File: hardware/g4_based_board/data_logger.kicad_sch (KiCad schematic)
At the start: 32 parts, among them J1 USB_C_Receptacle_USB2.0, SW1 SW_SPDT, SW2 RESET, U1 STM32G431CBTx, U2 AZ1117-3.3, Y1 12MHz, 20pF

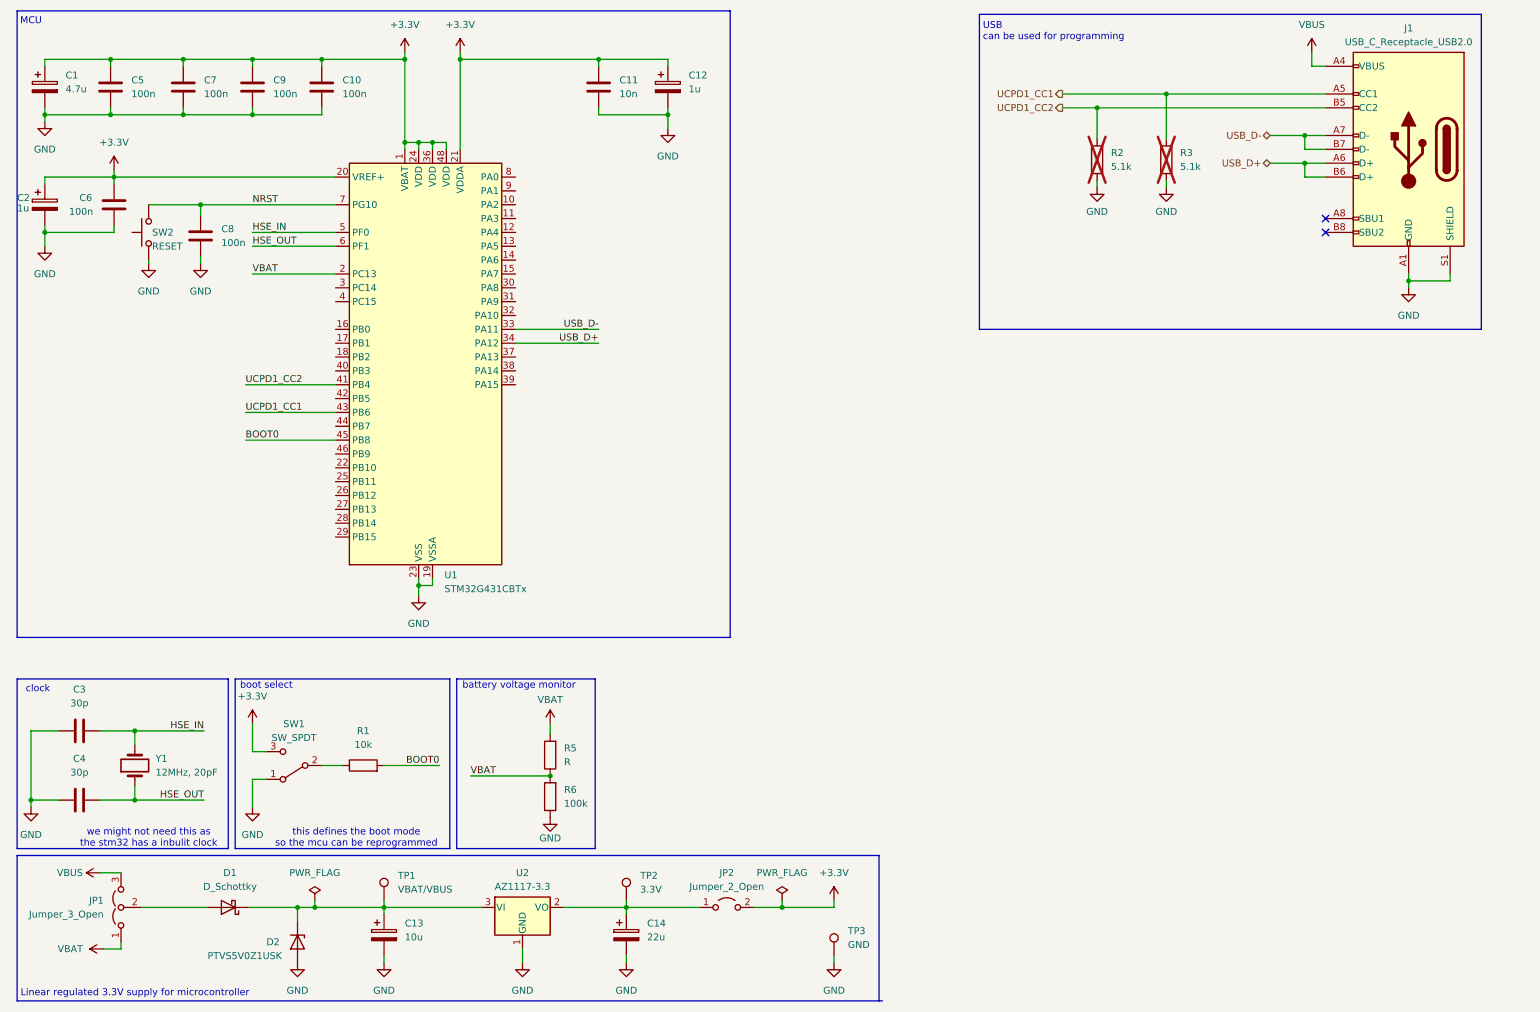
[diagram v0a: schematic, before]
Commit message: added auto updated files
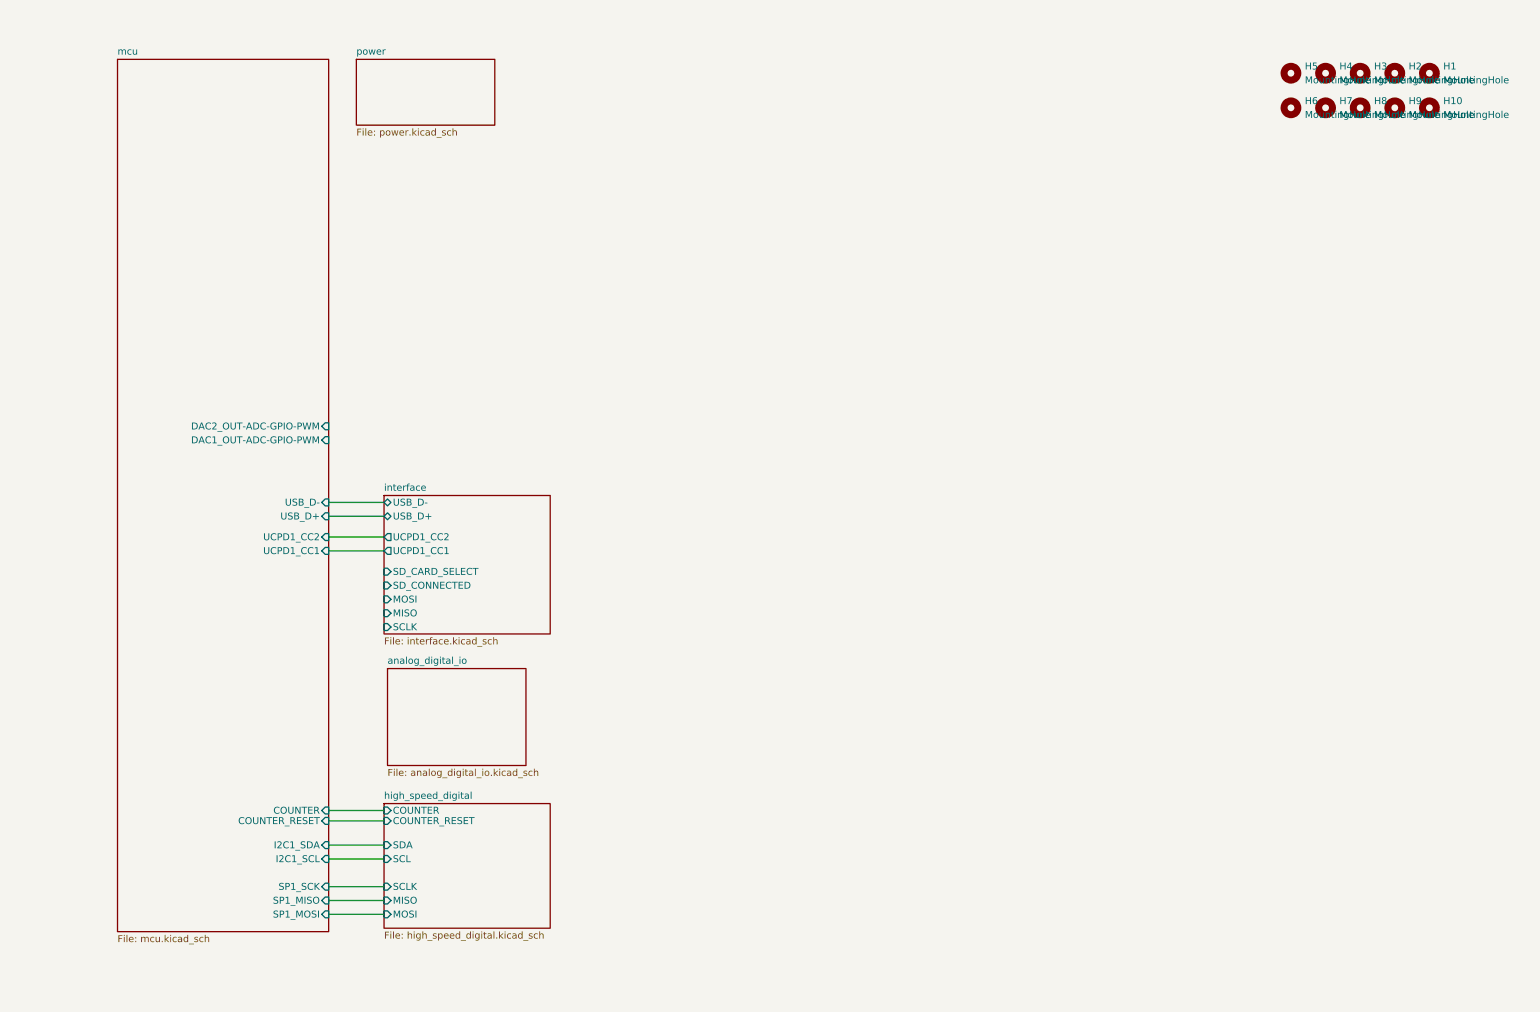
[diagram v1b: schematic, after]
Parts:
- removed C1: 4.7u, Capacitor_SMD:C_0805_2012Metric_Pad1.18x1.45mm_HandSolder, symbol Device:C_Polarized
- removed C10, C5, C6, C7, C8, C9: 100n, Capacitor_SMD:C_0805_2012Metric_Pad1.18x1.45mm_HandSolder, symbol Device:C
- removed C11: 10n, Capacitor_SMD:C_0805_2012Metric_Pad1.18x1.45mm_HandSolder, symbol Device:C
- removed C12, C2: 1u, Capacitor_SMD:C_0805_2012Metric_Pad1.18x1.45mm_HandSolder, symbol Device:C_Polarized
- removed C13: 10u, Capacitor_SMD:C_0805_2012Metric_Pad1.18x1.45mm_HandSolder, symbol Device:C_Polarized
- removed C14: 22u, Capacitor_SMD:C_0805_2012Metric_Pad1.18x1.45mm_HandSolder, symbol Device:C_Polarized
- removed C3, C4: 30p, Capacitor_SMD:C_0805_2012Metric_Pad1.18x1.45mm_HandSolder, symbol Device:C
- removed D1: D_Schottky, Diode_SMD:D_0805_2012Metric_Pad1.15x1.40mm_HandSolder, symbol Device:D_Schottky
- removed D2: PTVS5V0Z1USK, Diode_SMD:Nexperia_DSN1608-2_1.6x0.8mm, symbol Diode:PTVS5V0Z1USK
- removed J1: USB_C_Receptacle_USB2.0, Connector_USB:USB_C_Receptacle_HRO_TYPE-C-31-M-12, symbol Connector:USB_C_Receptacle_USB2.0
- removed JP1: Jumper_3_Open, Connector_PinHeader_2.54mm:PinHeader_1x03_P2.54mm_Vertical, symbol Jumper:Jumper_3_Open
- removed JP2: Jumper_2_Open, symbol Jumper:Jumper_2_Open
- removed R1: 10k, Resistor_SMD:R_0805_2012Metric_Pad1.20x1.40mm_HandSolder, symbol Device:R
- removed R2, R3: 5.1k, Resistor_SMD:R_0805_2012Metric_Pad1.20x1.40mm_HandSolder, symbol Device:R
- removed R5: R, Resistor_SMD:R_0805_2012Metric_Pad1.20x1.40mm_HandSolder, symbol Device:R
- removed R6: 100k, Resistor_SMD:R_0805_2012Metric_Pad1.20x1.40mm_HandSolder, symbol Device:R
- removed SW1: SW_SPDT, Button_Switch_THT:SW_Slide_SPDT_Angled_CK_OS102011MA1Q, symbol Switch:SW_SPDT
- removed SW2: RESET, Button_Switch_SMD:SW_Push_SPST_NO_Alps_SKRK, symbol Switch:SW_Push
- removed TP1: VBAT/VBUS, TestPoint:TestPoint_Pad_D1.5mm, symbol Connector:TestPoint
- removed TP2: 3.3V, TestPoint:TestPoint_Pad_D1.5mm, symbol Connector:TestPoint
- removed TP3: GND, TestPoint:TestPoint_Pad_D1.5mm, symbol Connector:TestPoint
- removed U1: STM32G431CBTx, Package_QFP:LQFP-48_7x7mm_P0.5mm, symbol MCU_ST_STM32G4:STM32G431CBTx
- removed U2: AZ1117-3.3, Package_TO_SOT_SMD:SOT-223, symbol Regulator_Linear:AZ1117-3.3
- removed Y1: 12MHz, 20pF, Crystal:Crystal_HC49-U_Vertical, symbol Device:Crystal
- added H1, H10, H2, H3, H4, H5, H6, H7, H8, H9: MountingHole, MountingHole:MountingHole_3.2mm_M3, symbol Mechanical:MountingHole
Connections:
- no-connect marks 2 -> 0
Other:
- added sheet analog_digital_io (analog_digital_io.kicad_sch)
- added sheet high_speed_digital (high_speed_digital.kicad_sch)
- added sheet interface (interface.kicad_sch)
- added sheet mcu (mcu.kicad_sch)
- added sheet power (power.kicad_sch)
- note removed: "Linear regulated 3.3V supply for microcontroller"
- note removed: "MCU"
- note removed: "USB can be used for programming"
- note removed: "battery voltage monitor"
- note removed: "boot select"
- note removed: "clock"
- note removed: "this defines the boot mode so the mcu can be reprogrammed"
- note removed: "we might not need this as the stm32 has a inbulit clock"

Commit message: auto updated files
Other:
- added sheet comms_interface (comms_interface.kicad_sch)
- added sheet thermalcouples (thermalcouples.kicad_sch)
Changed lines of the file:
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@@
 	)
 	(sheet
-		(at 76.2 22.86)
+		(at 80.645 46.355)
+		(size 30.48 22.225)
+		(fields_autoplaced yes)
+		(stroke
+			(width 0.1524)
+			(type solid)
+		)
+		(fill
+			(color 0 0 0 0.0000)
+		)
+		(property "Sheetname" "comms_interface"
+			(at 80.645 45.6434 0)
+			(effects
+				(font
+					(size 1.27 1.27)
+				)
+				(justify left bottom)
+			)
+		)
+		(property "Sheetfile" "comms_interface.kicad_sch"
+			(at 80.645 69.1646 0)
+			(effects
+				(font
+					(size 1.27 1.27)
+				)
+				(justify left top)
+			)
+		)
+		(instances
+			(project "data_logger"
+				(path "/9bc93932-ff5f-4f35-96cf-dfa5f042acb6"
+					(page "8")
+				)
+			)
+		)
+	)
+	(sheet
+		(at 80.645 24.13)
 		(size 25.4 12.065)
 		(fields_autoplaced yes)
@@
 		)
 		(property "Sheetname" "power"
-			(at 76.2 22.1484 0)
+			(at 80.645 23.4184 0)
 			(effects
 				(font
@@
 		)
 		(property "Sheetfile" "power.kicad_sch"
-			(at 76.2 35.5096 0)
+			(at 80.645 36.7796 0)
 			(effects
 				(font
@@
 				(path "/9bc93932-ff5f-4f35-96cf-dfa5f042acb6"
 					(page "3")
+				)
+			)
+		)
+	)
+	(sheet
+		(at 81.28 73.025)
+		(size 30.48 23.495)
+		(fields_autoplaced yes)
+		(stroke
+			(width 0.1524)
+			(type solid)
+		)
+		(fill
+			(color 0 0 0 0.0000)
+		)
+		(property "Sheetname" "thermalcouples"
+			(at 81.28 72.3134 0)
+			(effects
+				(font
+					(size 1.27 1.27)
+				)
+				(justify left bottom)
+			)
+		)
+		(property "Sheetfile" "thermalcouples.kicad_sch"
+			(at 81.28 97.1046 0)
+			(effects
+				(font
+					(size 1.27 1.27)
+				)
+				(justify left top)
+			)
+		)
+		(instances
+			(project "data_logger"
+				(path "/9bc93932-ff5f-4f35-96cf-dfa5f042acb6"
+					(page "7")
 				)
 			)
@@
 		)
 		(pin "DAC2_OUT-ADC-GPIO-PWM" input
-			(at 71.12 90.17 0)
+			(at 71.12 136.525 0)
 			(effects
 				(font
@@
 		)
 		(pin "DAC1_OUT-ADC-GPIO-PWM" input
-			(at 71.12 92.71 0)
-			(effects
-				(font
+			(at 71.12 139.065 0)
+			(effects
+				(font

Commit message: auto updated files
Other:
- removed sheet thermalcouples
- sheet analog_digital_io ports: added GPIO-1, GPIO-10, GPIO-11, GPIO-12, GPIO-2, GPIO-3, GPIO-4, GPIO-5, GPIO-6, GPIO-7, GPIO-8, GPIO-9; removed none
- sheet comms_interface ports: added COUNTER, RESET, SPI_CLK, SPI_MISO, SPI_MOSI; removed none
- sheet mcu ports: added ADC-GPIO-PWM-1-DIFF1-1, ADC-GPIO-PWM-10, ADC-GPIO-PWM-11, ADC-GPIO-PWM-12, ADC-GPIO-PWM-2-DIFF1-2, ADC-GPIO-PWM-3, ADC-GPIO-PWM-4, ADC-GPIO-PWM-5, ADC-GPIO-PWM-6, ADC-GPIO-PWM-7, ADC-GPIO-PWM-8, ADC-GPIO-PWM-9, COMMS_COUNTER, COMMS_SPI_CK, COMMS_SPI_MISO, COMMS_SPI_MOSI, SD_CARD_DETECT, SD_CARD_ENABLE; removed none

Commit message: auto updated kicad files
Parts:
- added J10, J13, J18, J8: Conn_01x07_Socket, Connector_PinHeader_2.54mm:PinHeader_1x07_P2.54mm_Vertical, symbol Connector:Conn_01x07_Socket
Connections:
- new net +3.3V: J10.2 (Pin_2)
- new net +5V: J10.1 (Pin_1), J13.1 (Pin_1)
- new net +BATT: J10.3 (Pin_3), J13.3 (Pin_3)
- new net +VDC: J10.4 (Pin_4), J13.4 (Pin_4)
- new net -VDC: J10.5 (Pin_5), J13.5 (Pin_5)
- new net GND: J10.6 (Pin_6), J10.7 (Pin_7), J13.2 (Pin_2), J13.7 (Pin_7), J18.7 (Pin_7), J8.7 (Pin_7)
- new net V_bat_monitor: J13.6 (Pin_6)
- new net interface/MISO: J8.2 (Pin_2)
- new net interface/MOSI: J8.3 (Pin_3)
- new net interface/SCLK: J8.1 (Pin_1)
- new net spi_en_expander/EN_10: J18.4 (Pin_4)
- new net spi_en_expander/EN_11: J18.5 (Pin_5)
- new net spi_en_expander/EN_12: J18.6 (Pin_6)
- new net spi_en_expander/EN_13: J8.5 (Pin_5)
- new net spi_en_expander/EN_14: J8.6 (Pin_6)
- new net spi_en_expander/EN_15: J8.4 (Pin_4)
- new net spi_en_expander/EN_7: J18.1 (Pin_1)
- new net spi_en_expander/EN_8: J18.2 (Pin_2)
- new net spi_en_expander/EN_9: J18.3 (Pin_3)
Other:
- removed sheet comms_interface
- added sheet spi_en_expander (spi_en_expander.kicad_sch)
- sheet analog_digital_io ports: added GPIO-1-DAC, GPIO-2-DAC; removed none
- sheet high_speed_digital ports: added EN_1, EN_2, EN_3, EN_4, EN_5, EN_6; removed COUNTER, COUNTER_RESET
- sheet mcu ports: added V_bat_monitor; removed COMMS_COUNTER, SD_CARD_ENABLE
- note added: "INPUT PWR Connector"
- note added: "OUTPUT PWR header"
- title: (none) -> top level view

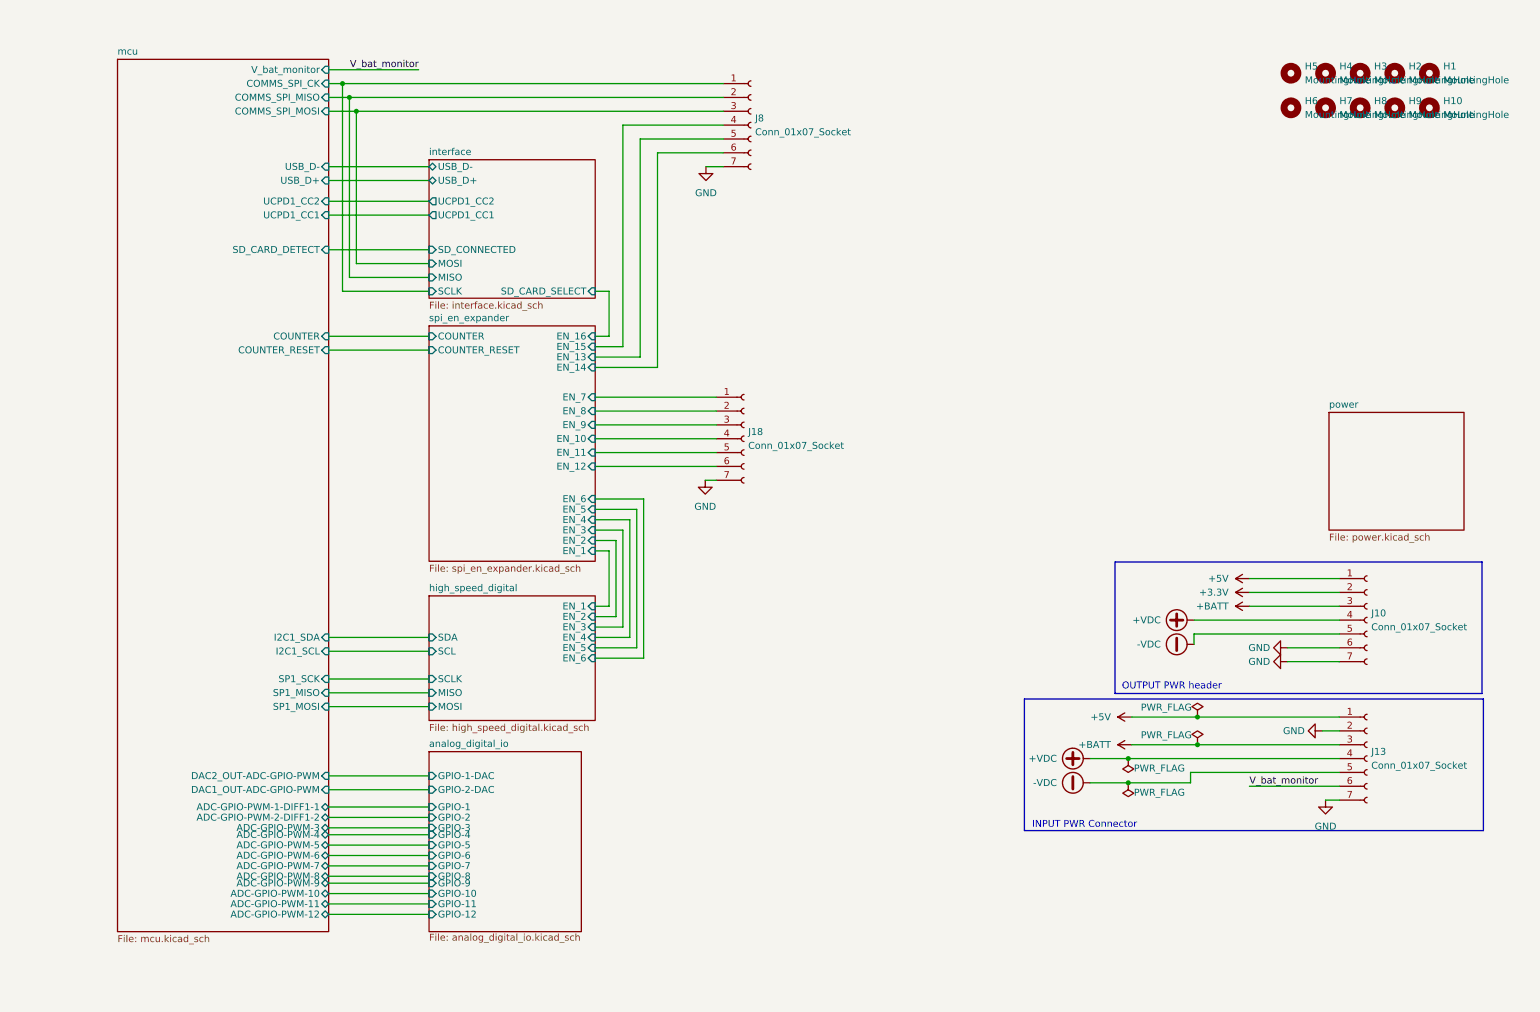
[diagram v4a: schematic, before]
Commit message: updated 5v in for the psu to +5P to distinguish between that and 5v for the pwoer switcher
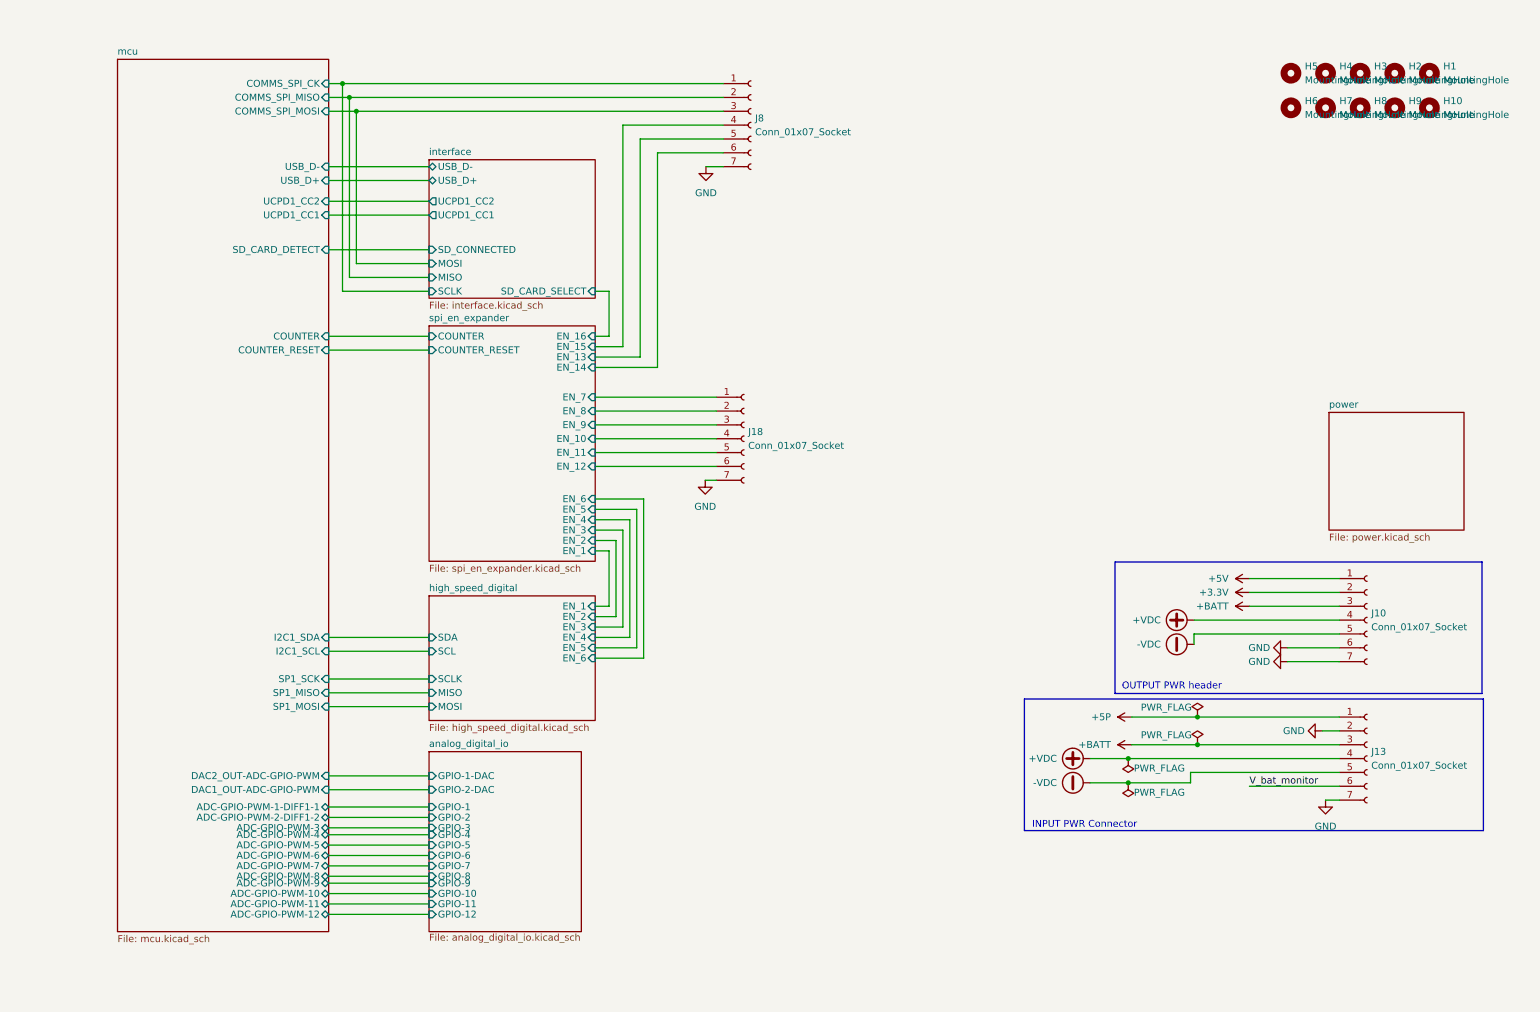
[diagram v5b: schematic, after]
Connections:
- net +5V: no longer J13.1 (Pin_1)
- new net +5P: J13.1 (Pin_1)
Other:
- sheet mcu ports: added none; removed V_bat_monitor
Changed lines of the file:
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@@
 	(wire
 		(pts
-			(xy 87.63 24.765) (xy 71.12 24.765)
-		)
-		(stroke
-			(width 0)
-			(type default)
-		)
-	)
-	(wire
-		(pts
 			(xy 71.12 57.785) (xy 89.535 57.785)
 		)
@@
 	)
 	(label "V_bat_monitor"
-		(at 87.63 24.765 180)
-		(fields_autoplaced yes)
-		(effects
-			(font
-				(size 1.27 1.27)
-			)
-			(justify right bottom)
-		)
-	)
-	(label "V_bat_monitor"
 		(at 240.03 156.21 0)
 		(fields_autoplaced yes)
@@
 	)
 	(symbol
-		(lib_id "power:+5V")
+		(lib_id "power:+5P")
 		(at 218.44 143.51 90)
 		(unit 1)
@@
 			)
 		)
-		(property "Value" "+5V"
+		(property "Value" "+5P"
 			(at 214.63 143.5099 90)
 			(effects
@@
 			)
 		)
-		(property "Description" "Power symbol creates a global label with name \"+5V\""
+		(property "Description" "Power symbol creates a global label with name \"+5P\""
 			(at 218.44 143.51 0)
 			(effects
@@
 			(effects
 				(font
-					(size 1.27 1.27)
-				)
-				(justify right)
-			)
-		)
-		(pin "V_bat_monitor" input
-			(at 71.12 24.765 0)
-			(effects
-				(font

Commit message: auto updated files
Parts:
- removed J18: Conn_01x07_Socket, Connector_PinHeader_2.54mm:PinHeader_1x07_P2.54mm_Vertical, symbol Connector:Conn_01x07_Socket
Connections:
- net spi_en_expander/EN_13 renamed mcu/COMMS_EN_2
- net spi_en_expander/EN_14 renamed mcu/COMMS_EN_3
- net spi_en_expander/EN_15 renamed mcu/COMMS_EN_1
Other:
- removed sheet spi_en_expander
- sheet mcu ports: added COMMS_EN_1, COMMS_EN_2, COMMS_EN_3, DIGITAL_IO_EN_1, DIGITAL_IO_EN_2, DIGITAL_IO_EN_3, DIGITAL_IO_EN_4, DIGITAL_IO_EN_5, DIGITAL_IO_EN_6, PWR_STATUS, SD_CARD_EN, VBATT_MONITOR; removed COUNTER, COUNTER_RESET
- sheet power ports: added PWR_STATUS; removed none

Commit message: auto updated
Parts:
- removed J10: Conn_01x07_Socket, Connector_PinHeader_2.54mm:PinHeader_1x07_P2.54mm_Vertical, symbol Connector:Conn_01x07_Socket
- added J2: Conn_02x07_Odd_Even, Connector_PinHeader_2.54mm:PinHeader_2x07_P2.54mm_Vertical, symbol Connector_Generic:Conn_02x07_Odd_Even
- renumbered H5 to H1, H6 to H2, H4 to H3, H7 to H4, H3 to H5, H8 to H6, H2 to H7, H9 to H8, H1 to H9, J8 to J1, J13 to J3
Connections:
- net +3.3V: now also J2.3 (Pin_3), J2.4 (Pin_4)
- net +5V: now also J2.1 (Pin_1), J2.2 (Pin_2)
- net +BATT: now also J2.5 (Pin_5), J2.6 (Pin_6)
- net +VDC: now also J2.7 (Pin_7), J2.8 (Pin_8)
- net -VDC: now also J2.10 (Pin_10), J2.9 (Pin_9)
- net GND: now also J2.11 (Pin_11), J2.12 (Pin_12), J2.13 (Pin_13), J2.14 (Pin_14)
